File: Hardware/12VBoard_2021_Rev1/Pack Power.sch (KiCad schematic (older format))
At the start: 10 parts, among them U1 LM2576SX-5.0/NOPB

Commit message: kiCad was erroring out when it didnt need to
also changed anderson to horizontal side by side.
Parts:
- Conn3: footprint MRDT_Connectors:Anderson_2_Horizontal_Stacked -> MRDT_Connectors:Anderson_2_Horizontal_Side_by_Side
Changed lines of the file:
@@
 EESchema Schematic File Version 4
+LIBS:12VBoard_2021_Rev1-cache
 EELAYER 30 0
 EELAYER END
@@
 F 0 "Conn3" H 5148 2967 60  0000 C CNN
 F 1 "PackVoltage" H 5148 2861 60  0000 C CNN
-F 2 "MRDT_Connectors:Anderson_2_Horizontal_Stacked" H 4790 2030 60  0001 C CNN
+F 2 "MRDT_Connectors:Anderson_2_Horizontal_Side_by_Side" H 4790 2030 60  0001 C CNN
 F 3 "" H 4790 2030 60  0001 C CNN
 	1    4940 2580
@@
 F 0 "Conn3" H 5158 3437 60  0000 C CNN
 F 1 "PackVoltage" H 5158 3331 60  0000 C CNN
-F 2 "MRDT_Connectors:Anderson_2_Horizontal_Stacked" H 4800 2500 60  0001 C CNN
+F 2 "MRDT_Connectors:Anderson_2_Horizontal_Side_by_Side" H 4800 2500 60  0001 C CNN
 F 3 "" H 4800 2500 60  0001 C CNN
 	2    4950 3050

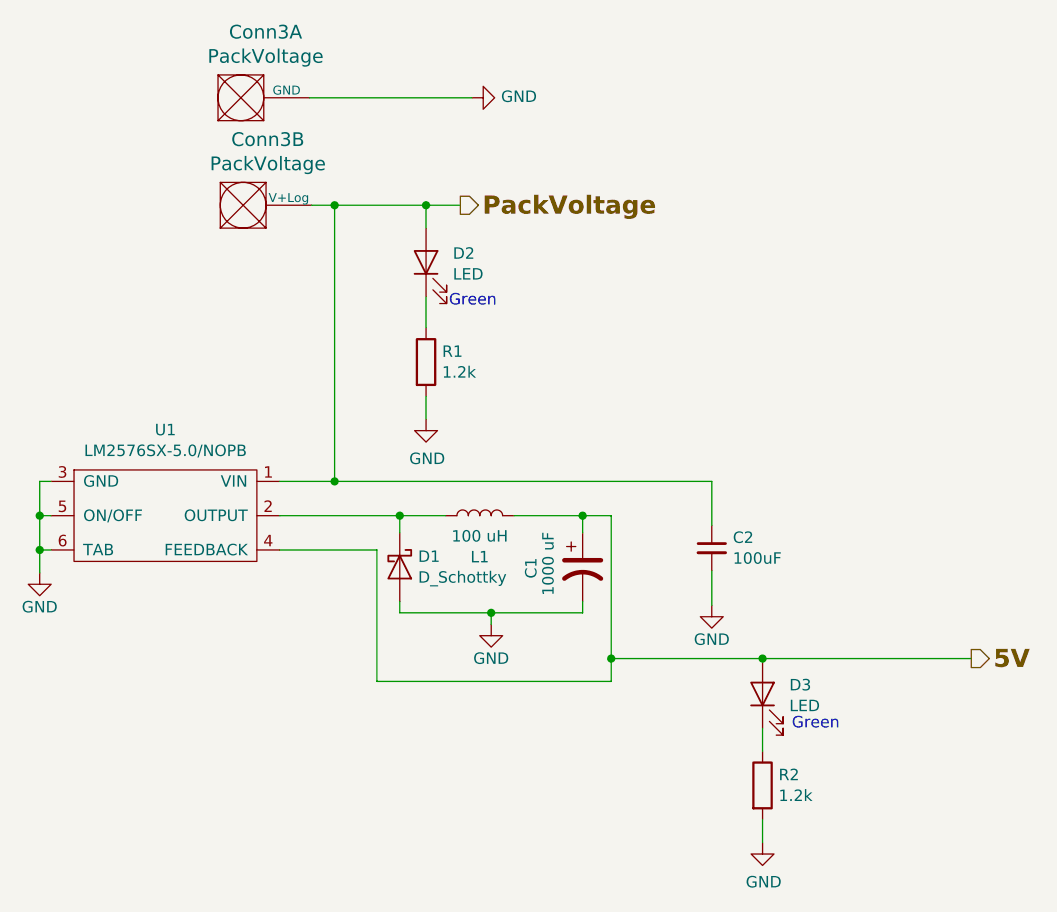
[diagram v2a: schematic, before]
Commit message: Worked on layout
Low current bucks grouped with their componets
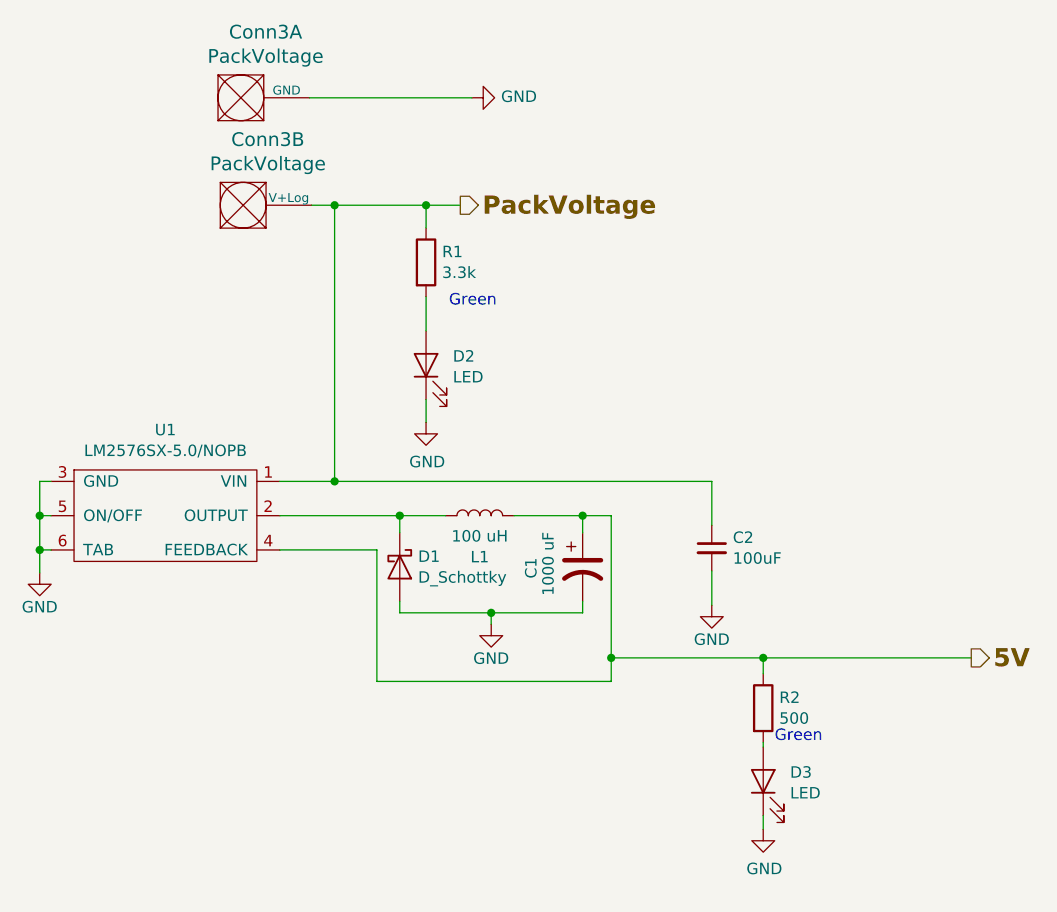
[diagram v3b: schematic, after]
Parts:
- C1: footprint Capacitor_THT:CP_Axial_L20.0mm_D10.0mm_P26.00mm_Horizontal -> Capacitor_THT:CP_Radial_D10.0mm_P5.00mm
- R1: value 1.2k -> 3.3k
- R2: value 1.2k -> 500
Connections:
- net 5V: now also R2.1; no longer D3.2 (A)
- net GND: now also D2.1 (K), D3.1 (K); no longer R1.2, R2.2
- net PackVoltage: now also R1.1; no longer D2.2 (A)
- new net: D2.2 (A), R1.2
- new net: D3.2 (A), R2.2
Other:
- moved on the sheet: D2, D3, R1, R2
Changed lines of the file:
@@
 EESchema Schematic File Version 4
-LIBS:12VBoard_2021_Rev1-cache
 EELAYER 30 0
 EELAYER END
@@
 Comment4 ""
 $EndDescr
-Text HLabel 8235 4933 2    79   Output ~ 16
+Text HLabel 8235 4930 2    79   Output ~ 16
 5V
 $Comp
@@
 $EndComp
 Wire Wire Line
-	6660 4933 6660 5033
-Connection ~ 6660 4933
-Wire Wire Line
-	8235 4933 7322 4933
-Wire Wire Line
 	5635 5033 6660 5033
 Wire Wire Line
@@
 	5210 4458 5635 4458
 Connection ~ 6535 4308
-Wire Wire Line
-	6660 4308 6660 4933
 Wire Wire Line
 	6535 4308 6660 4308
@@
 F 0 "C1" V 6310 4483 50  0000 L CNN
 F 1 "1000 uF" V 6385 4408 50  0000 L CNN
-F 2 "Capacitor_THT:CP_Axial_L20.0mm_D10.0mm_P26.00mm_Horizontal" H 6535 4533 50  0001 C CNN
+F 2 "Capacitor_THT:CP_Radial_D10.0mm_P5.00mm" H 6535 4533 50  0001 C CNN
 F 3 "~" H 6535 4533 50  0001 C CNN
 	1    6535 4533
@@
 L Device:R R?
 U 1 1 5F9524D1
-P 5850 3636
+P 5850 3200
 AR Path="/5F74F36B/5F821EB2/5F9524D1" Ref="R?"  Part="1"
 AR Path="/5F74F36B/5F8236F9/5F9524D1" Ref="R?"  Part="1"
 AR Path="/5F8031F1/5F9524D1" Ref="R1"  Part="1"
-F 0 "R1" H 5920 3682 50  0000 L CNN
-F 1 "1.2k" H 5920 3591 50  0000 L CNN
-F 2 "Resistor_SMD:R_0603_1608Metric_Pad1.05x0.95mm_HandSolder" V 5780 3636 50  0001 C CNN
-F 3 "~" H 5850 3636 50  0001 C CNN
-	1    5850 3636
+F 0 "R1" H 5920 3246 50  0000 L CNN
+F 1 "3.3k" H 5920 3155 50  0000 L CNN
+F 2 "Resistor_SMD:R_0603_1608Metric_Pad1.05x0.95mm_HandSolder" V 5780 3200 50  0001 C CNN
+F 3 "~" H 5850 3200 50  0001 C CNN
+	1    5850 3200
 	1    0    0    -1
 $EndComp
@@
 L power:GND #PWR?
 U 1 1 5F9524D7
-P 5850 3886
+P 5850 3900
 AR Path="/5F74F36B/5F821EB2/5F9524D7" Ref="#PWR?"  Part="1"
 AR Path="/5F74F36B/5F8236F9/5F9524D7" Ref="#PWR?"  Part="1"
 AR Path="/5F8031F1/5F9524D7" Ref="#PWR02"  Part="1"
-F 0 "#PWR02" H 5850 3636 50  0001 C CNN
-F 1 "GND" H 5855 3713 50  0000 C CNN
-F 2 "" H 5850 3886 50  0001 C CNN
-F 3 "" H 5850 3886 50  0001 C CNN
-	1    5850 3886
+F 0 "#PWR02" H 5850 3650 50  0001 C CNN
+F 1 "GND" H 5855 3727 50  0000 C CNN
+F 2 "" H 5850 3900 50  0001 C CNN
+F 3 "" H 5850 3900 50  0001 C CNN
+	1    5850 3900
 	1    0    0    -1
 $EndComp
@@
 L Device:LED D?
 U 1 1 5F9524DD
-P 5850 3200
+P 5850 3650
 AR Path="/5F74F36B/5F821EB2/5F9524DD" Ref="D?"  Part="1"
 AR Path="/5F74F36B/5F8236F9/5F9524DD" Ref="D?"  Part="1"
 AR Path="/5F8031F1/5F9524DD" Ref="D2"  Part="1"
-F 0 "D2" V 5889 3083 50  0000 R CNN
-F 1 "LED" V 5798 3083 50  0000 R CNN
-F 2 "Diode_SMD:D_0603_1608Metric_Pad1.05x0.95mm_HandSolder" H 5850 3200 50  0001 C CNN
-F 3 "~" H 5850 3200 50  0001 C CNN
-	1    5850 3200
+F 0 "D2" V 5889 3533 50  0000 R CNN
+F 1 "LED" V 5798 3533 50  0000 R CNN
+F 2 "Diode_SMD:D_0603_1608Metric_Pad1.05x0.95mm_HandSolder" H 5850 3650 50  0001 C CNN
+F 3 "~" H 5850 3650 50  0001 C CNN
+	1    5850 3650
 	0    -1   -1   0
 $EndComp
-Wire Wire Line
-	5850 3886 5850 3786
 $Comp
 L power:GND #PWR03
@@
 PackVoltage
 $Comp
-L Device:R R?
-U 1 1 5F96E7E8
-P 7322 5488
-AR Path="/5F74F36B/5F821EB2/5F96E7E8" Ref="R?"  Part="1"
-AR Path="/5F74F36B/5F8236F9/5F96E7E8" Ref="R?"  Part="1"
-AR Path="/5F8031F1/5F96E7E8" Ref="R2"  Part="1"
-F 0 "R2" H 7392 5534 50  0000 L CNN
-F 1 "1.2k" H 7392 5443 50  0000 L CNN
-F 2 "Resistor_SMD:R_0603_1608Metric_Pad1.05x0.95mm_HandSolder" V 7252 5488 50  0001 C CNN
-F 3 "~" H 7322 5488 50  0001 C CNN
-	1    7322 5488
-	1    0    0    -1
-$EndComp
-$Comp
-L power:GND #PWR?
-U 1 1 5F96E7EE
-P 7322 5738
-AR Path="/5F74F36B/5F821EB2/5F96E7EE" Ref="#PWR?"  Part="1"
-AR Path="/5F74F36B/5F8236F9/5F96E7EE" Ref="#PWR?"  Part="1"
-AR Path="/5F8031F1/5F96E7EE" Ref="#PWR06"  Part="1"
-F 0 "#PWR06" H 7322 5488 50  0001 C CNN
-F 1 "GND" H 7327 5565 50  0000 C CNN
-F 2 "" H 7322 5738 50  0001 C CNN
-F 3 "" H 7322 5738 50  0001 C CNN
-	1    7322 5738
-	1    0    0    -1
-$EndComp
-$Comp
 L Device:LED D?
 U 1 1 5F96E7F4
-P 7322 5088
+P 7325 5470
 AR Path="/5F74F36B/5F821EB2/5F96E7F4" Ref="D?"  Part="1"
 AR Path="/5F74F36B/5F8236F9/5F96E7F4" Ref="D?"  Part="1"
 AR Path="/5F8031F1/5F96E7F4" Ref="D3"  Part="1"
-F 0 "D3" V 7361 4971 50  0000 R CNN
-F 1 "LED" V 7270 4971 50  0000 R CNN
-F 2 "Diode_SMD:D_0603_1608Metric_Pad1.05x0.95mm_HandSolder" H 7322 5088 50  0001 C CNN
-F 3 "~" H 7322 5088 50  0001 C CNN
-	1    7322 5088
+F 0 "D3" V 7364 5353 50  0000 R CNN
+F 1 "LED" V 7273 5353 50  0000 R CNN
+F 2 "Diode_SMD:D_0603_1608Metric_Pad1.05x0.95mm_HandSolder" H 7325 5470 50  0001 C CNN
+F 3 "~" H 7325 5470 50  0001 C CNN
+	1    7325 5470
 	0    -1   -1   0
 $EndComp
-Wire Wire Line
-	7322 5738 7322 5638
-Wire Wire Line
-	7322 5338 7322 5238
-Wire Wire Line
-	7322 4933 7322 4938
-Connection ~ 7322 4933
-Wire Wire Line
-	7322 4933 6660 4933
 $Comp
 L Device:C_Small C2
@@
 Text Notes 5950 3400 0    50   ~ 0
 Green
-Text Notes 7450 5250 0    50   ~ 0
+Text Notes 7375 5305 0    50   ~ 0
 Green
-Wire Wire Line
-	5850 3350 5850 3486
 Wire Wire Line
 	5350 2950 5450 2950
@@
 	1    0    0    -1
 $EndComp
+Wire Wire Line
+	5850 3350 5850 3500
+Wire Wire Line
+	5850 3800 5850 3900
+$Comp
+L Device:R R?
+U 1 1 5F96E7E8
+P 7325 5150
+AR Path="/5F74F36B/5F821EB2/5F96E7E8" Ref="R?"  Part="1"
+AR Path="/5F74F36B/5F8236F9/5F96E7E8" Ref="R?"  Part="1"
+AR Path="/5F8031F1/5F96E7E8" Ref="R2"  Part="1"
+F 0 "R2" H 7395 5196 50  0000 L CNN
+F 1 "500" H 7395 5105 50  0000 L CNN
+F 2 "Resistor_SMD:R_0603_1608Metric_Pad1.05x0.95mm_HandSolder" V 7255 5150 50  0001 C CNN
+F 3 "~" H 7325 5150 50  0001 C CNN
+	1    7325 5150
+	1    0    0    -1
+$EndComp
+Wire Wire Line
+	6660 4308 6660 4930
+Wire Wire Line
+	8235 4930 7325 4930
+Connection ~ 6660 4930
+Wire Wire Line
+	6660 4930 6660 5033
+Wire Wire Line
+	7325 5000 7325 4930
+Connection ~ 7325 4930
+Wire Wire Line
+	7325 4930 6660 4930
+Wire Wire Line
+	7325 5300 7325 5320
+$Comp
+L power:GND #PWR?
+U 1 1 5F96E7EE
+P 7325 5680
+AR Path="/5F74F36B/5F821EB2/5F96E7EE" Ref="#PWR?"  Part="1"
+AR Path="/5F74F36B/5F8236F9/5F96E7EE" Ref="#PWR?"  Part="1"
+AR Path="/5F8031F1/5F96E7EE" Ref="#PWR06"  Part="1"
+F 0 "#PWR06" H 7325 5430 50  0001 C CNN
+F 1 "GND" H 7330 5507 50  0000 C CNN
+F 2 "" H 7325 5680 50  0001 C CNN
+F 3 "" H 7325 5680 50  0001 C CNN
+	1    7325 5680
+	1    0    0    -1
+$EndComp
+Wire Wire Line
+	7325 5620 7325 5680
 $EndSCHEMATC

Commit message: updated footprints
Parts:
- D1: footprint Diode_SMD:D_0603_1608Metric_Pad1.05x0.95mm_HandSolder -> Diode_THT:D_DO-201AD_P15.24mm_Horizontal
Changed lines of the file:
@@
 F 0 "D1" V 5689 4613 50  0000 L CNN
 F 1 "D_Schottky" V 5780 4613 50  0000 L CNN
-F 2 "Diode_SMD:D_0603_1608Metric_Pad1.05x0.95mm_HandSolder" H 5735 4533 50  0001 C CNN
+F 2 "Diode_THT:D_DO-201AD_P15.24mm_Horizontal" H 5735 4533 50  0001 C CNN
 F 3 "~" H 5735 4533 50  0001 C CNN
 	1    5735 4533

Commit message: Made Silkscreen Boxes
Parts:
- D1: footprint Diode_THT:D_DO-201AD_P15.24mm_Horizontal -> Diode_THT:D_DO-201AD_P5.08mm_Vertical_KathodeUp
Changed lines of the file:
@@
 F 0 "D1" V 5689 4613 50  0000 L CNN
 F 1 "D_Schottky" V 5780 4613 50  0000 L CNN
-F 2 "Diode_THT:D_DO-201AD_P15.24mm_Horizontal" H 5735 4533 50  0001 C CNN
+F 2 "Diode_THT:D_DO-201AD_P5.08mm_Vertical_KathodeUp" H 5735 4533 50  0001 C CNN
 F 3 "~" H 5735 4533 50  0001 C CNN
 	1    5735 4533

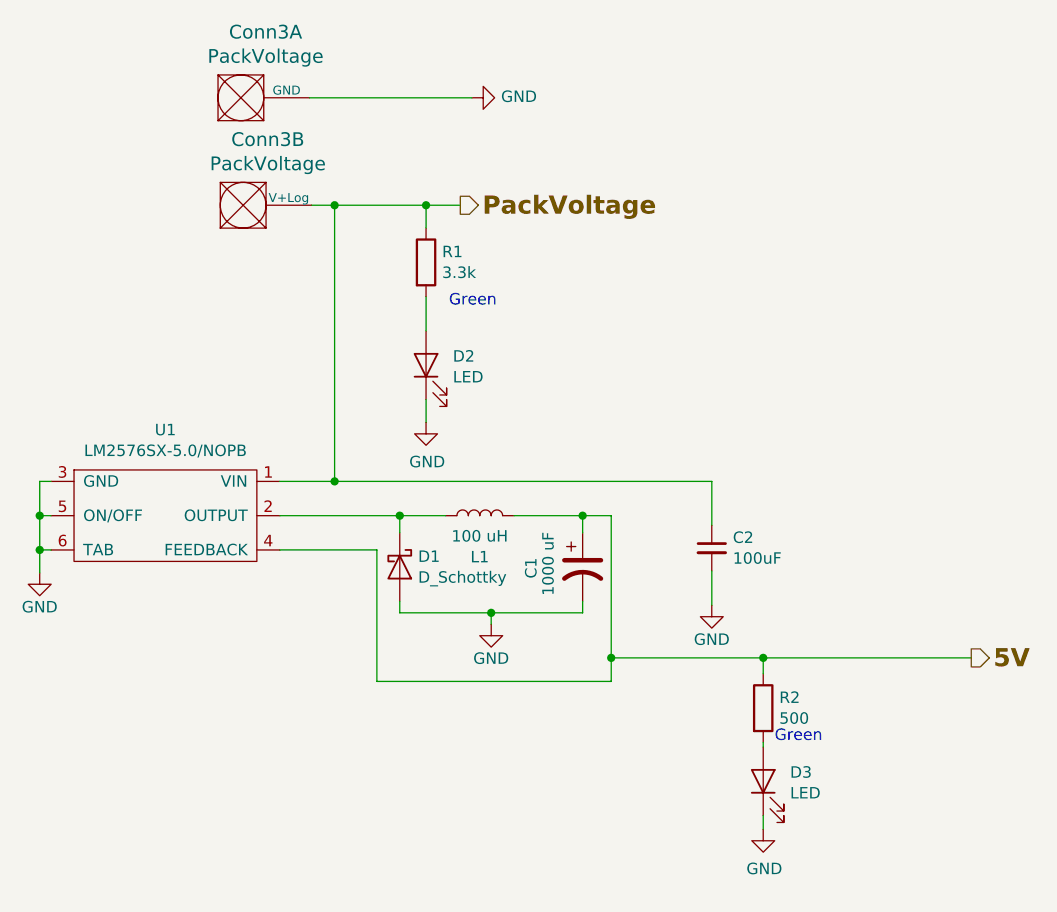
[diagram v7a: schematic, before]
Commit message: Aded oki and started change of high side logic setup
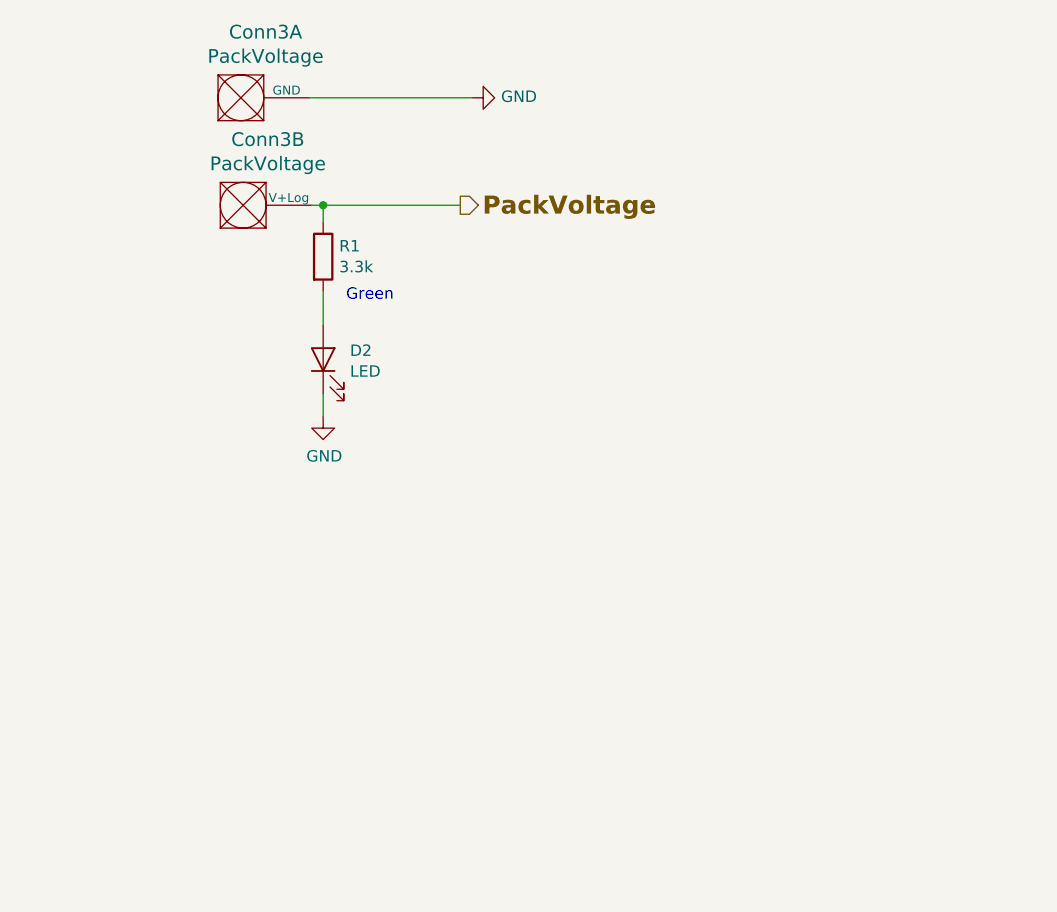
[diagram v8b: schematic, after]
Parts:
- removed C1: 1000 uF, Capacitor_THT:CP_Radial_D10.0mm_P5.00mm, symbol Device:CP1
- removed C2: 100uF, Capacitor_SMD:C_0603_1608Metric_Pad1.05x0.95mm_HandSolder, symbol Device:C_Small
- removed D1: D_Schottky, Diode_THT:D_DO-201AD_P5.08mm_Vertical_KathodeUp, symbol Device:D_Schottky
- removed D3: LED, Diode_SMD:D_0603_1608Metric_Pad1.05x0.95mm_HandSolder, symbol Device:LED
- removed L1: 100 uH, Inductor_SMD:L_0603_1608Metric_Pad1.05x0.95mm_HandSolder, symbol Device:L
- removed R2: 500, Resistor_SMD:R_0603_1608Metric_Pad1.05x0.95mm_HandSolder, symbol Device:R
- removed U1: LM2576SX-5.0/NOPB, MRDT_Devices:LM2576, symbol 12VBoard_2021_Rev1-rescue:LM2576D2TR4-MRDT_Devices
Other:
- moved on the sheet: D2, R1
